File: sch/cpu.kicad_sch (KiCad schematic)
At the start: 10 parts

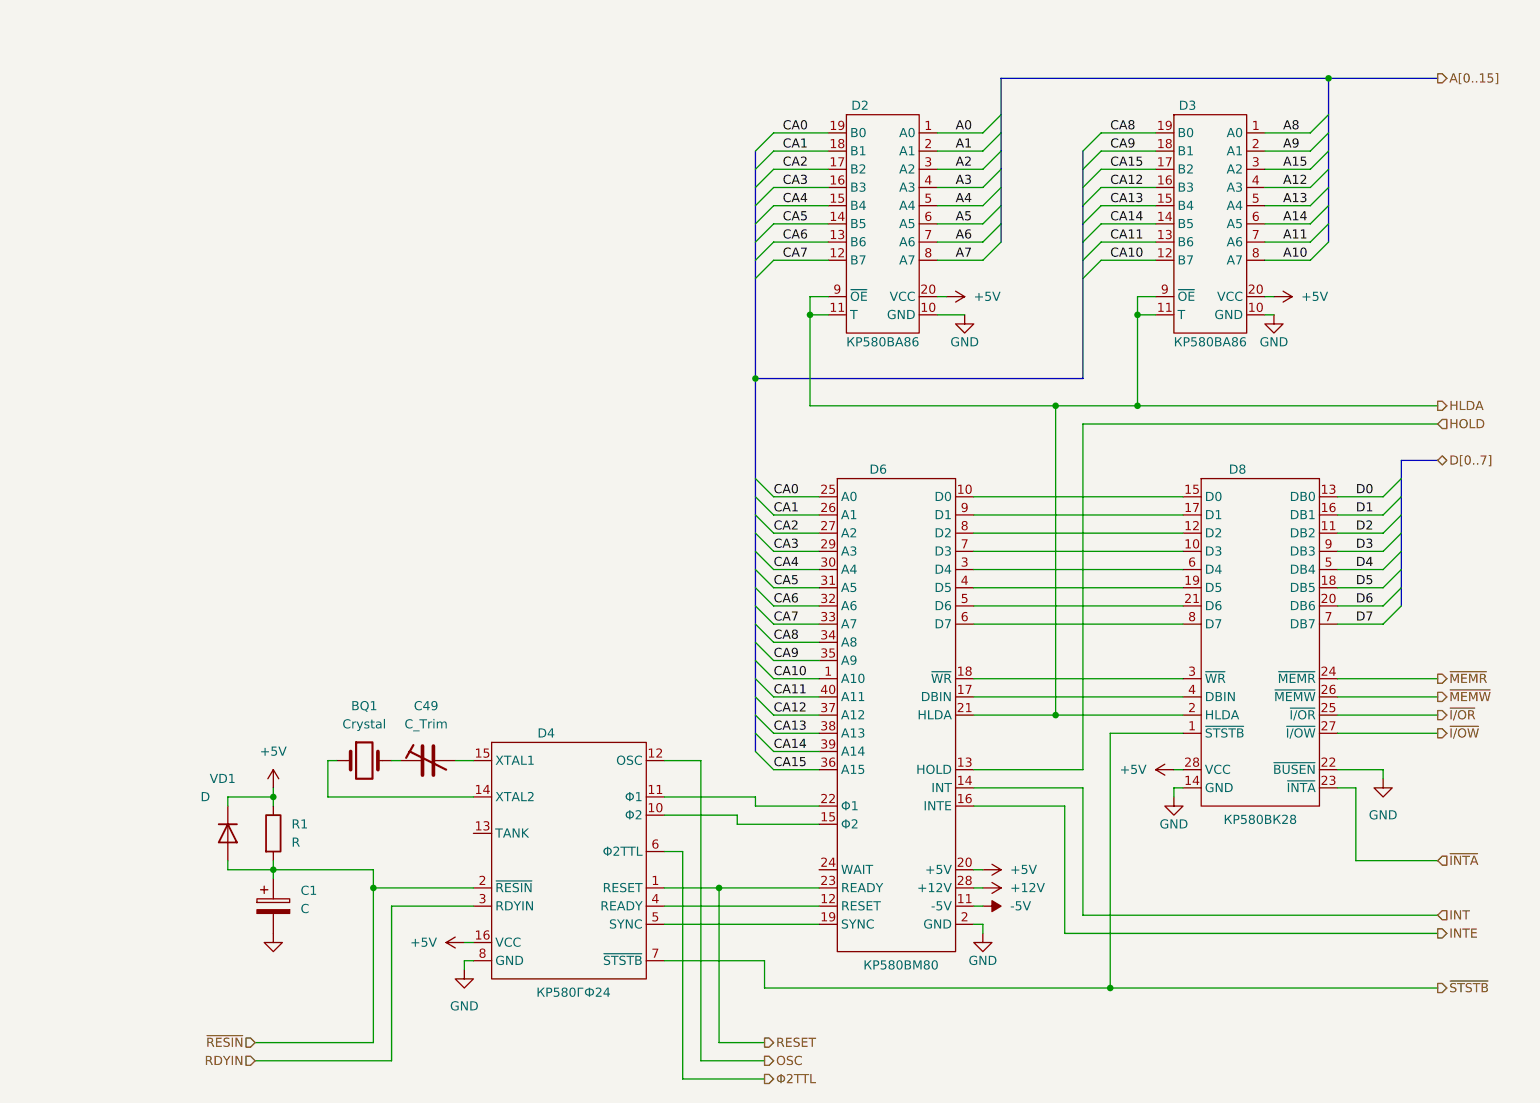
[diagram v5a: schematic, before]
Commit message: Sch: video block cleanup in progress
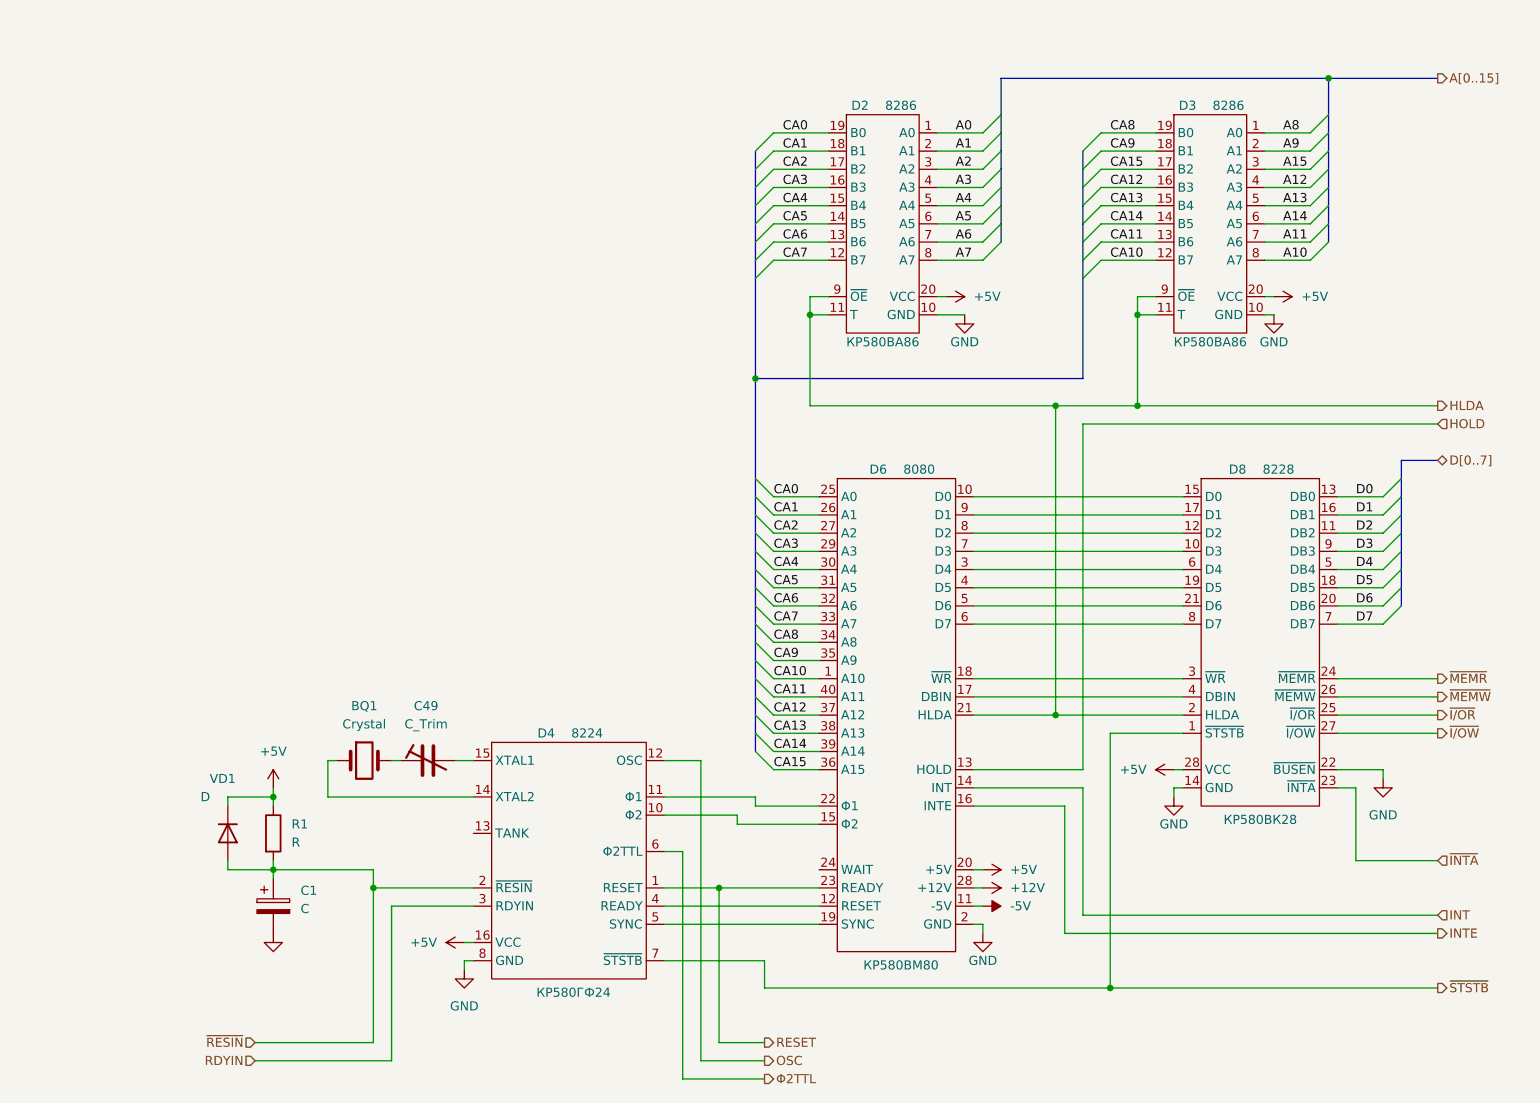
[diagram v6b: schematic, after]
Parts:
- D2, D3: value (none) -> 8286
- D4: value (none) -> 8224
- D6: value (none) -> 8080
- D8: value (none) -> 8228
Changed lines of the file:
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@@
     (in_bom yes) (on_board yes)
     (property "Reference" "D4" (id 0) (at 93.98 118.11 0))
-    (property "Value" "" (id 1) (at 99.695 118.11 0))
+    (property "Value" "8224" (id 1) (at 99.695 118.11 0))
     (property "Footprint" "" (id 2) (at 86.36 119.38 0)
       (effects (font (size 1.27 1.27)) hide)
@@
     (in_bom yes) (on_board yes)
     (property "Reference" "D8" (id 0) (at 190.5 81.28 0))
-    (property "Value" "" (id 1) (at 196.215 81.28 0))
+    (property "Value" "8228" (id 1) (at 196.215 81.28 0))
     (property "Footprint" "" (id 2) (at 185.42 81.28 0)
       (effects (font (size 1.27 1.27)) hide)
@@
     (in_bom yes) (on_board yes)
     (property "Reference" "D3" (id 0) (at 183.515 30.48 0))
-    (property "Value" "" (id 1) (at 189.23 30.48 0))
+    (property "Value" "8286" (id 1) (at 189.23 30.48 0))
     (property "Footprint" "" (id 2) (at 181.61 31.75 0)
       (effects (font (size 1.27 1.27)) hide)
@@
     (in_bom yes) (on_board yes)
     (property "Reference" "D6" (id 0) (at 140.335 81.28 0))
-    (property "Value" "" (id 1) (at 146.05 81.28 0))
+    (property "Value" "8080" (id 1) (at 146.05 81.28 0))
     (property "Footprint" "" (id 2) (at 134.62 82.55 0)
       (effects (font (size 1.27 1.27)) hide)
@@
     (in_bom yes) (on_board yes)
     (property "Reference" "D2" (id 0) (at 137.795 30.48 0))
-    (property "Value" "" (id 1) (at 143.51 30.48 0))
+    (property "Value" "8286" (id 1) (at 143.51 30.48 0))
     (property "Footprint" "" (id 2) (at 135.89 31.75 0)
       (effects (font (size 1.27 1.27)) hide)

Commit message: Sch: CPU block cleanup
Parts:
- BQ1: value Crystal -> 20MHz
- C1: value C -> 50μF
- C49: value C_Trim -> 4/20pF
- R1: value R -> 2k7
- VD1: value D -> КД522Б
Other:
- moved on the sheet: BQ1, C1, C49, D2, D3, D4, D6, D8, R1, VD1

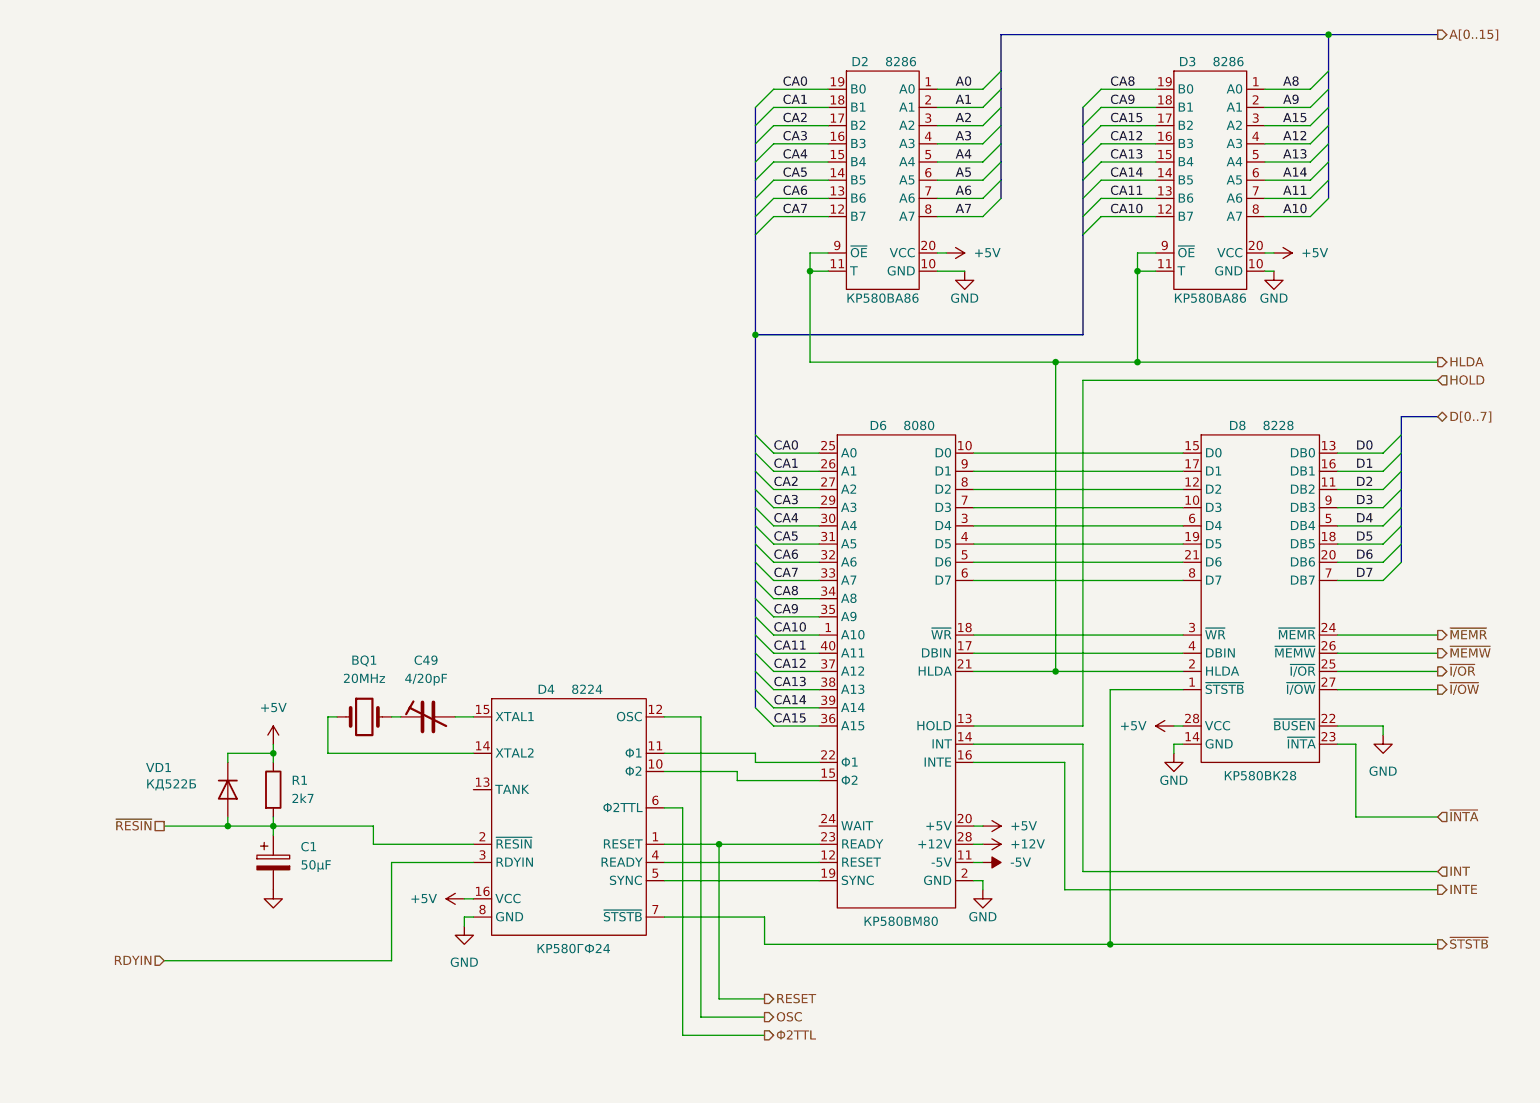
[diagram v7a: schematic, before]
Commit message: Sch:  CPU - added wait state injection FF
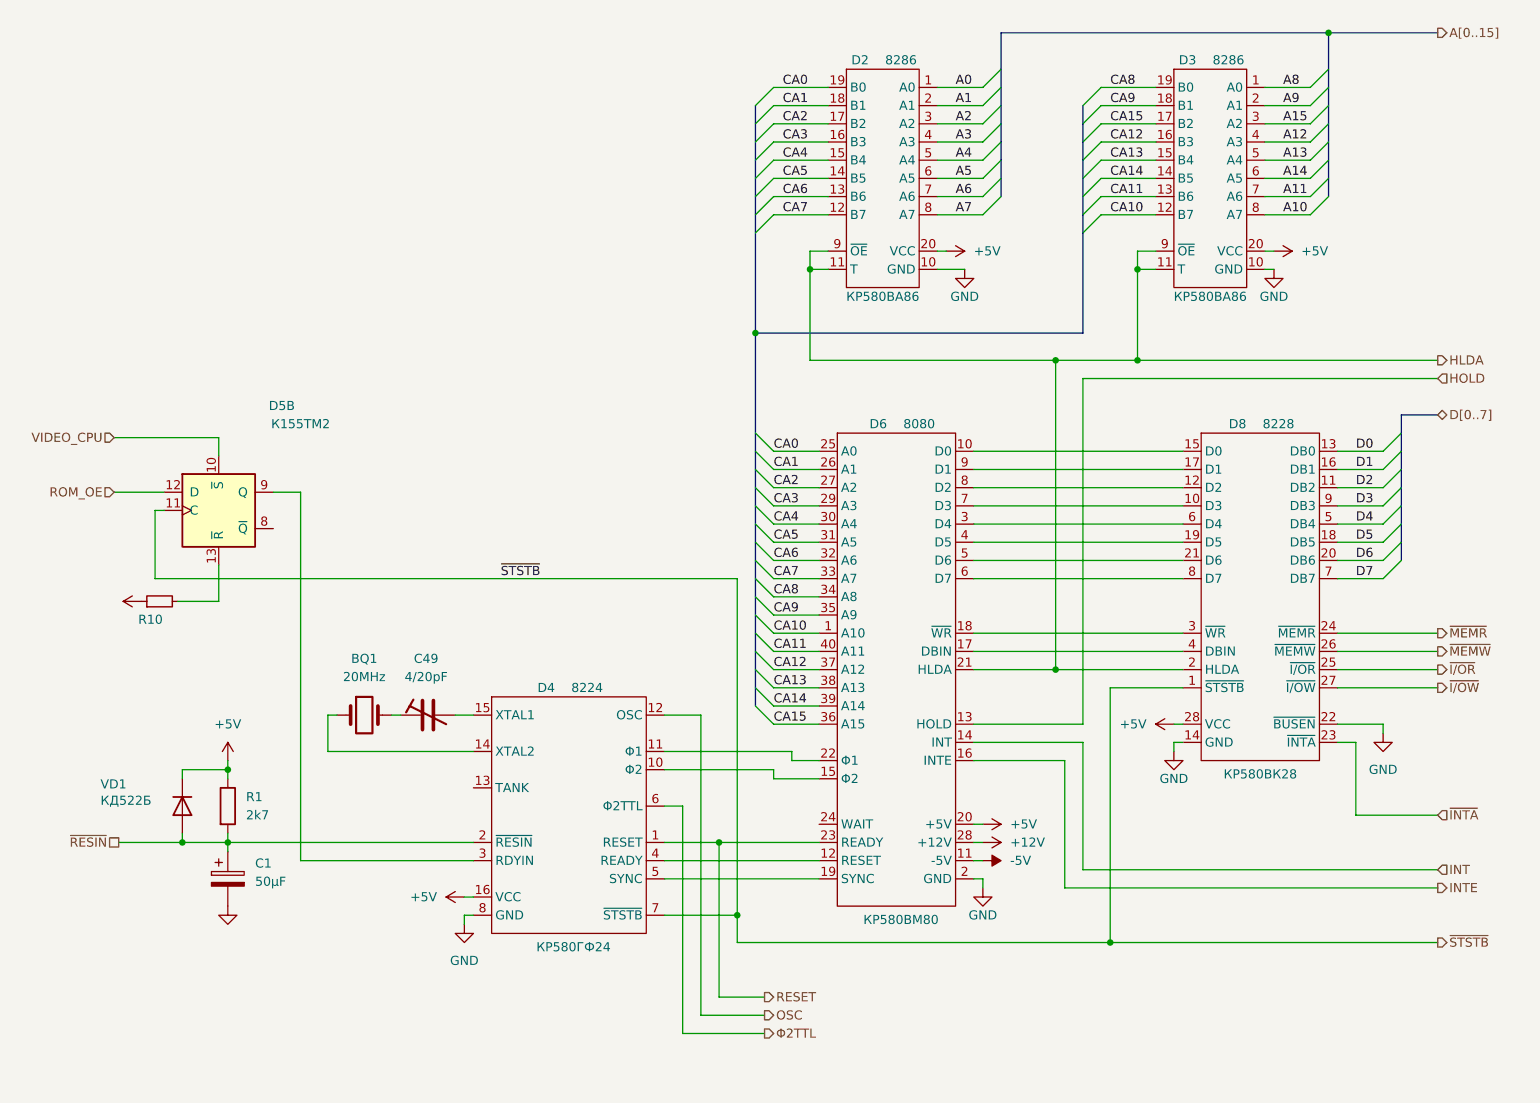
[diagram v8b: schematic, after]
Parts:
- added D5: (no value), symbol 74xx:74LS74
- added R10: (no value), symbol Device:R_Small
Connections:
- net +5V: now also R10.1
- net ~{STSTB}: now also D5.11 (C)
- net RDYIN: no longer names the net of D4.3 (RDYIN)
- net RDYIN: now also D5.9 (Q)
- new net: D5.13 (~{R}), R10.2
- new net ROM_OE: D5.12 (D)
- new net VIDEO_CPU: D5.10 (~{S})
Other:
- moved on the sheet: C1, R1, VD1
